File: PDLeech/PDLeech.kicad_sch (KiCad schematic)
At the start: 12 parts

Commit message: schematic finished
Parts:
- removed R?: 270k, -Passive:R_0603, symbol -Passive:R
- removed R?: 51k, -Passive:R_0603, symbol -Passive:R
- added Q1, Q2, Q3, Q4: BSS84, Package_TO_SOT_SMD:SOT-23, symbol Transistor_FET:BSS84
- added R1, R2: 1k, symbol Device:R
- added R3: 270k, symbol Device:R
- added R4: 51k, symbol Device:R
- gave numbers to parts that had none: 10
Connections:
- net +5V: now also R3.1
- net GND: now also R4.2
- net CC2_IN: now reaches JP2.1 (A), P1.B5 (VCONN)
- net CC2_IN: now also Q3.3 (D), R2.1
- net CC2_OUT: now reaches J1.B5 (CC2), JP2.2 (C)
- net CC2_OUT: now also Q4.3 (D)
- net CC2_G: now reaches JP2.3 (B)
- net CC2_G: now also Q3.1 (G), Q4.1 (G), R2.2
- net at U1.5 (FB): now also R3.2, R4.1
- net CC1_OUT: now reaches J1.A5 (CC1), JP1.2 (C)
- net CC1_OUT: now also Q2.3 (D)
- net D+: now reaches J1.A6 (D+), J1.B6 (D+), P1.A6 (D+)
- net D+: now also J2.3 (D+)
- net D-: now reaches J1.A7 (D-), J1.B7 (D-), P1.A7 (D-)
- net D-: now also J2.2 (D-)
- net CC1_IN: now reaches JP1.1 (A), P1.A5 (CC)
- net CC1_IN: now also Q1.3 (D), R1.1
- net CC1_G: now reaches JP1.3 (B)
- net CC1_G: now also Q1.1 (G), Q2.1 (G), R1.2
- new net: Q1.2 (S), Q2.2 (S)
- new net: Q3.2 (S), Q4.2 (S)
- no-connect marks 3 -> 1
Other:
- note removed: "add switching circuit"
- moved on the sheet: C1, C2, C3, J1, J2, JP1, JP2, L1, P1, U1

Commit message: updated schematic
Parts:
- removed R1: 1k, symbol Device:R
- added R?: 4.1k, symbol Device:R
- added R? (x2): 1k, symbol Device:R
- R2: value 1k -> 4.1k
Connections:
- net CC1_G: now also R?.1; no longer Q1.1 (G), Q2.1 (G)
- net CC2_G: now also R2.1; no longer Q3.1 (G), Q4.1 (G), R2.2
- net CC2_IN: no longer R2.1
- net GND: now also R?.2, R?.2
- new net: Q1.1 (G), Q2.1 (G), R?.1, R?.2
- new net: Q3.1 (G), Q4.1 (G), R2.2, R?.1
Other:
- moved on the sheet: Q1, Q2, Q3, Q4, R2

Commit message: added some footprtints
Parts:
- J1: footprint (none) -> Connector_USB:USB_C_Receptacle_Amphenol_12401548E4-2A
- J2: footprint (none) -> USB-A:SAMTEC_USB-A-S-X-X-SM2
- JP1, JP2: footprint (none) -> Jumper:SolderJumper-3_P1.3mm_Bridged12_RoundedPad1.0x1.5mm_NumberLabels
- R1, R2, R4: renamed from R?; footprint (none) -> Resistor_SMD:R_0603_1608Metric_Pad0.98x0.95mm_HandSolder
- R3: renamed from R2; footprint (none) -> Resistor_SMD:R_0603_1608Metric_Pad0.98x0.95mm_HandSolder
- R5: renamed from R3; footprint (none) -> Resistor_SMD:R_0603_1608Metric_Pad0.98x0.95mm_HandSolder
- R6: renamed from R4; footprint (none) -> Resistor_SMD:R_0603_1608Metric_Pad0.98x0.95mm_HandSolder

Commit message: selected all footprints
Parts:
- J1: value USB_C_Receptacle -> TYPEC-324DBW-ACP24A
- P1: value USB_C_Plug -> U261-241N-4BC2LS; footprint (none) -> type-c_plug:USB-C-SMD_XKB_U261-241N-4BC2LS
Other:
- note added: "https://www.lcsc.com/product-detail/USB-Connectors_XKB-Connectivity-U261-241N-4BC2LS_C2880648.html"
- note added: "https://www.lcsc.com/product-detail/USB-Connectors_XUNPU-TYPEC-324DBW-ACP24A_C2840399.html"
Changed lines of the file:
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@@
+    (stroke (width 0) (type default) (color 0 0 0 0))
+  )
+  (wire (pts (xy 22.225 32.385) (xy 23.495 32.385))
     (stroke (width 0) (type default) (color 0 0 0 0))
   )
@@
     (stroke (width 0) (type default) (color 0 0 0 0))
   )
+  (wire (pts (xy 80.645 32.385) (xy 81.915 32.385))
+    (stroke (width 0) (type default) (color 0 0 0 0))
+  )
   (wire (pts (xy 53.34 64.135) (xy 53.34 56.515))
     (stroke (width 0) (type default) (color 0 0 0 0))
@@
   (wire (pts (xy 161.925 72.39) (xy 161.925 74.93))
     (stroke (width 0) (type default) (color 0 0 0 0))
+  )
+  (text "https://www.lcsc.com/product-detail/USB-Connectors_XKB-Connectivity-U261-241N-4BC2LS_C2880648.html"
+    (at 17.78 133.35 0)
+    (effects (font (size 1.27 1.27)) (justify left bottom))
+  )
+  (text "https://www.lcsc.com/product-detail/USB-Connectors_XUNPU-TYPEC-324DBW-ACP24A_C2840399.html"
+    (at 17.78 135.89 0)
+    (effects (font (size 1.27 1.27)) (justify left bottom))
   )
   (text "5V 500mA\n" (at 230.124 48.895 0)
@@
     (effects (font (size 1.27 1.27)) (justify left bottom))
   )
-  (label "CC1_G" (at 23.495 32.385 180)
+  (label "CC1_G" (at 22.225 32.385 180)
     (effects (font (size 1.27 1.27)) (justify right bottom))
   )
-  (label "CC2_G" (at 81.915 32.385 180)
+  (label "CC2_G" (at 80.645 32.385 180)
     (effects (font (size 1.27 1.27)) (justify right bottom))
   )
@@
       (effects (font (size 1.27 1.27)) (justify right))
     )
-    (property "Value" "USB_C_Receptacle" (id 1) (at 104.902 89.5349 0)
+    (property "Value" "TYPEC-324DBW-ACP24A" (id 1) (at 104.902 89.5349 0)
       (effects (font (size 1.27 1.27)) (justify right))
     )
@@
   (symbol (lib_id "-Flag:GND") (at 161.925 76.835 0) (unit 1)
     (in_bom yes) (on_board yes)
-    (property "Reference" "#PWR?" (id 0) (at 161.925 83.185 0)
+    (property "Reference" "#PWR0101" (id 0) (at 161.925 83.185 0)
       (effects (font (size 1.27 1.27)) hide)
     )
@@
     (in_bom yes) (on_board yes) (fields_autoplaced)
     (property "Reference" "P1" (id 0) (at 35.56 51.435 0))
-    (property "Value" "USB_C_Plug" (id 1) (at 35.56 53.975 0))
-    (property "Footprint" "" (id 2) (at 39.37 84.455 0)
+    (property "Value" "U261-241N-4BC2LS" (id 1) (at 35.56 53.975 0))
+    (property "Footprint" "type-c_plug:USB-C-SMD_XKB_U261-241N-4BC2LS" (id 2) (at 39.37 84.455 0)
       (effects (font (size 1.27 1.27)) hide)
     )
@@
     )
     (path "/f0992a04-2738-491f-b5f0-0488ff8c2969"
-      (reference "#PWR?") (unit 1) (value "GND") (footprint "")
+      (reference "#PWR0101") (unit 1) (value "GND") (footprint "")
     )
     (path "/989225e2-7f6b-44a6-8e8d-13851093044b"
@@
     )
     (path "/369f8716-8ba2-4915-a138-c29ccad268b8"
-      (reference "J1") (unit 1) (value "USB_C_Receptacle") (footprint "Connector_USB:USB_C_Receptacle_Amphenol_12401548E4-2A")
+      (reference "J1") (unit 1) (value "TYPEC-324DBW-ACP24A") (footprint "Connector_USB:USB_C_Receptacle_Amphenol_12401548E4-2A")
     )
     (path "/4f67c36c-9553-4237-a40b-64d4286f5052"
@@
     )
     (path "/f8fbfb29-176e-4094-83b6-73d673cd805f"
-      (reference "P1") (unit 1) (value "USB_C_Plug") (footprint "")
+      (reference "P1") (unit 1) (value "U261-241N-4BC2LS") (footprint "type-c_plug:USB-C-SMD_XKB_U261-241N-4BC2LS")
     )
     (path "/f356469c-c44f-4f6c-baed-20c76f284af0"

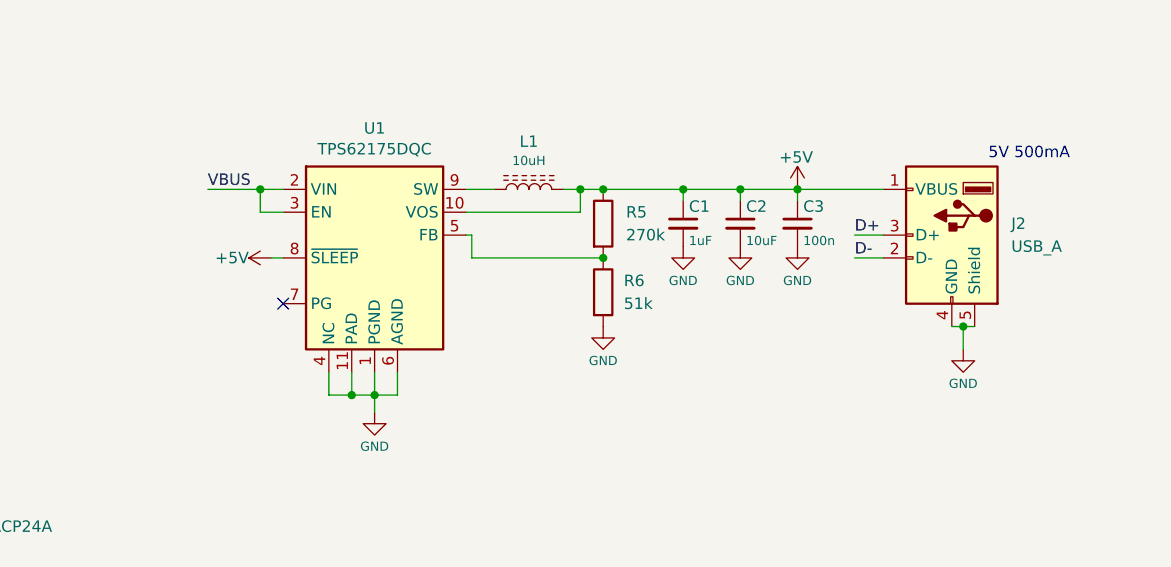
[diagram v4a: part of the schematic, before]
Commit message: schematic complete and footprints selected
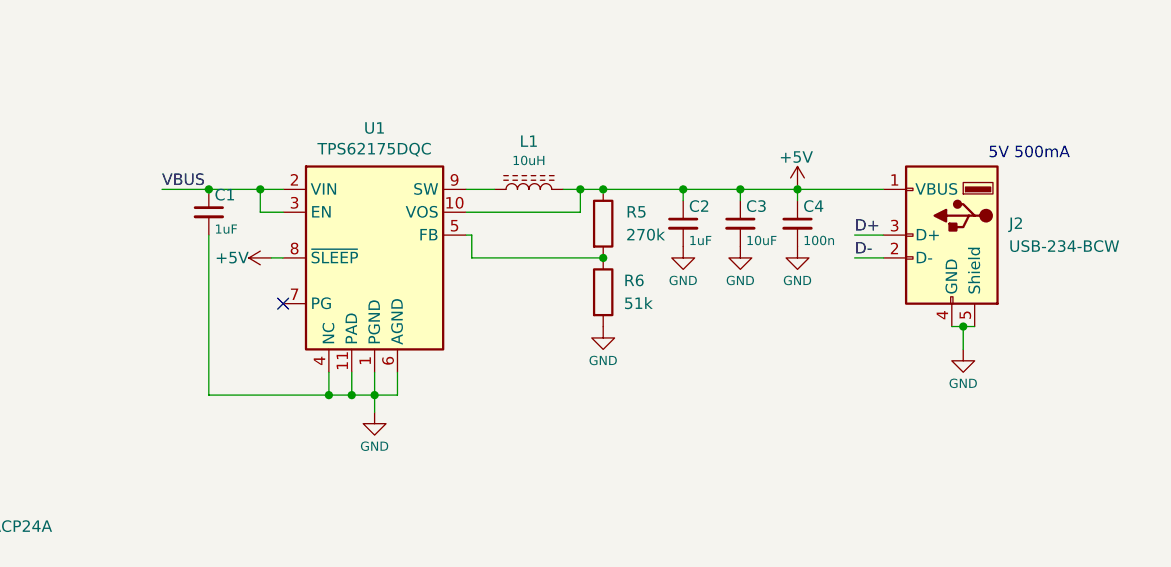
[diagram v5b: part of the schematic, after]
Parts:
- added C1: 1uF, Capacitor_SMD:C_0805_2012Metric_Pad1.18x1.45mm_HandSolder, symbol -Passive:C
- C2: renamed from C1; footprint -Passive:C_0805 -> Capacitor_SMD:C_0805_2012Metric_Pad1.18x1.45mm_HandSolder
- C3: renamed from C2; footprint -Passive:C_0805 -> Capacitor_SMD:C_0805_2012Metric_Pad1.18x1.45mm_HandSolder
- C4: renamed from C3; footprint -Passive:C_0805 -> Capacitor_SMD:C_0805_2012Metric_Pad1.18x1.45mm_HandSolder
- J2: value USB_A -> USB-234-BCW
- L1: footprint -Passive:L_4012 -> Ind-4012:L_4012
- U1: footprint -Chip:WSON-10-1EP_2x3mm_P0.5mm_EP0.84x2.4mm -> TPS62175DQC:WSON-10-1EP_2x3mm_P0.5mm_EP0.84x2.4mm
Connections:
- net GND: now also C1.2
- net VBUS: now also C1.1
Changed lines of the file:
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@@
   (junction (at 196.215 52.07) (diameter 0) (color 0 0 0 0)
   )
+  (junction (at 156.845 74.93) (diameter 0) (color 0 0 0 0)
+  )
   (junction (at 208.915 52.07) (diameter 0) (color 0 0 0 0)
   )
@@
   )
   (junction (at 63.5 125.095) (diameter 0) (color 0 0 0 0)
+  )
+  (junction (at 143.51 52.07) (diameter 0) (color 0 0 0 0)
   )
   (junction (at 95.25 32.385) (diameter 0) (color 0 0 0 0)
@@
     (stroke (width 0) (type default) (color 0 0 0 0))
   )
+  (wire (pts (xy 143.51 74.93) (xy 156.845 74.93))
+    (stroke (width 0) (type default) (color 0 0 0 0))
+  )
   (wire (pts (xy 50.8 64.135) (xy 53.34 64.135))
     (stroke (width 0) (type default) (color 0 0 0 0))
@@
     (stroke (width 0) (type default) (color 0 0 0 0))
   )
-  (wire (pts (xy 143.383 52.07) (xy 149.225 52.07))
+  (wire (pts (xy 138.303 52.07) (xy 143.51 52.07))
     (stroke (width 0) (type default) (color 0 0 0 0))
   )
@@
     (stroke (width 0) (type default) (color 0 0 0 0))
   )
+  (wire (pts (xy 143.51 52.07) (xy 149.225 52.07))
+    (stroke (width 0) (type default) (color 0 0 0 0))
+  )
   (wire (pts (xy 99.695 32.385) (xy 112.395 32.385))
     (stroke (width 0) (type default) (color 0 0 0 0))
@@
   )
   (wire (pts (xy 78.74 71.755) (xy 78.74 74.295))
+    (stroke (width 0) (type default) (color 0 0 0 0))
+  )
+  (wire (pts (xy 143.51 57.15) (xy 143.51 74.93))
     (stroke (width 0) (type default) (color 0 0 0 0))
   )
@@
     (effects (font (size 1.27 1.27)) (justify left bottom))
   )
-  (label "VBUS" (at 143.383 52.07 0)
+  (label "VBUS" (at 138.303 52.07 0)
     (effects (font (size 1.27 1.27)) (justify left bottom))
   )
@@
     (property "Reference" "U1" (id 0) (at 161.925 45.2882 0))
     (property "Value" "TPS62175DQC" (id 1) (at 161.925 47.5996 0))
-    (property "Footprint" "-Chip:WSON-10-1EP_2x3mm_P0.5mm_EP0.84x2.4mm" (id 2) (at 165.735 71.12 0)
+    (property "Footprint" "TPS62175DQC:WSON-10-1EP_2x3mm_P0.5mm_EP0.84x2.4mm" (id 2) (at 165.735 71.12 0)
       (effects (font (size 1.27 1.27)) (justify left) hide)
     )
@@
   (symbol (lib_id "-Passive:C") (at 208.915 55.88 0) (unit 1)
     (in_bom yes) (on_board yes)
-    (property "Reference" "C3" (id 0) (at 209.55 53.975 0)
+    (property "Reference" "C4" (id 0) (at 209.55 53.975 0)
       (effects (font (size 1.27 1.27)) (justify left))
     )
@@
       (effects (font (size 1.016 1.016)) (justify left))
     )
-    (property "Footprint" "-Passive:C_0805" (id 2) (at 209.8802 59.69 0)
+    (property "Footprint" "Capacitor_SMD:C_0805_2012Metric_Pad1.18x1.45mm_HandSolder" (id 2) (at 209.8802 59.69 0)
       (effects (font (size 1.27 1.27)) hide)
     )
     (property "Datasheet" "~" (id 3) (at 208.915 55.88 0)
+      (effects (font (size 1.27 1.27)) hide)
+    )
+    (pin "1")
+    (pin "2")
+  )
+  (symbol (lib_id "-Passive:C") (at 143.51 54.61 0) (unit 1)
+    (in_bom yes) (on_board yes)
+    (property "Reference" "C1" (id 0) (at 144.145 52.705 0)
+      (effects (font (size 1.27 1.27)) (justify left))
+    )
+    (property "Value" "1uF" (id 1) (at 144.145 56.515 0)
+      (effects (font (size 1.016 1.016)) (justify left))
+    )
+    (property "Footprint" "Capacitor_SMD:C_0805_2012Metric_Pad1.18x1.45mm_HandSolder" (id 2) (at 144.4752 58.42 0)
+      (effects (font (size 1.27 1.27)) hide)
+    )
+    (property "Datasheet" "~" (id 3) (at 143.51 54.61 0)
       (effects (font (size 1.27 1.27)) hide)
     )
@@
   (symbol (lib_id "Connector:USB_A") (at 226.06 57.15 0) (mirror y) (unit 1)
     (in_bom yes) (on_board yes) (fields_autoplaced)
-    (property "Reference" "J2" (id 0) (at 232.664 55.8799 0)
+    (property "Reference" "J2" (id 0) (at 232.41 55.8799 0)
       (effects (font (size 1.27 1.27)) (justify right))
     )
-    (property "Value" "USB_A" (id 1) (at 232.664 58.4199 0)
+    (property "Value" "USB-234-BCW" (id 1) (at 232.41 58.4199 0)
       (effects (font (size 1.27 1.27)) (justify right))
     )
@@
   (symbol (lib_id "-Passive:C") (at 196.215 55.88 0) (unit 1)
     (in_bom yes) (on_board yes)
-    (property "Reference" "C1" (id 0) (at 196.85 53.975 0)
+    (property "Reference" "C2" (id 0) (at 196.85 53.975 0)
       (effects (font (size 1.27 1.27)) (justify left))
     )
@@
       (effects (font (size 1.016 1.016)) (justify left))
     )
-    (property "Footprint" "-Passive:C_0805" (id 2) (at 197.1802 59.69 0)
+    (property "Footprint" "Capacitor_SMD:C_0805_2012Metric_Pad1.18x1.45mm_HandSolder" (id 2) (at 197.1802 59.69 0)
       (effects (font (size 1.27 1.27)) hide)
     )
@@
   (symbol (lib_id "-Passive:C") (at 202.565 55.88 0) (unit 1)
     (in_bom yes) (on_board yes)
-    (property "Reference" "C2" (id 0) (at 203.2 53.975 0)
+    (property "Reference" "C3" (id 0) (at 203.2 53.975 0)
       (effects (font (size 1.27 1.27)) (justify left))
     )
@@
       (effects (font (size 1.016 1.016)) (justify left))
     )
-    (property "Footprint" "-Passive:C_0805" (id 2) (at 203.5302 59.69 0)
+    (property "Footprint" "Capacitor_SMD:C_0805_2012Metric_Pad1.18x1.45mm_HandSolder" (id 2) (at 203.5302 59.69 0)
       (effects (font (size 1.27 1.27)) hide)
     )
@@
   (symbol (lib_id "-Flag:GND") (at 161.925 76.835 0) (unit 1)
     (in_bom yes) (on_board yes)
-    (property "Reference" "#PWR0101" (id 0) (at 161.925 83.185 0)
+    (property "Reference" "#PWR05" (id 0) (at 161.925 83.185 0)
       (effects (font (size 1.27 1.27)) hide)
     )
@@
       (effects (font (size 1.016 1.016)))
     )
-    (property "Footprint" "-Passive:L_4012" (id 2) (at 179.07 52.07 90)
+    (property "Footprint" "Ind-4012:L_4012" (id 2) (at 179.07 52.07 90)
       (effects (font (size 1.27 1.27)) hide)
     )
@@
       (reference "#PWR04") (unit 1) (value "+5V") (footprint "")
     )
+    (path "/f0992a04-2738-491f-b5f0-0488ff8c2969"
+      (reference "#PWR05") (unit 1) (value "GND") (footprint "")
+    )
     (path "/b7fa6ec7-c498-419b-95e2-74f90d037e3f"
       (reference "#PWR06") (unit 1) (value "GND") (footprint "")
@@
       (reference "#PWR011") (unit 1) (value "GND") (footprint "")
     )
-    (path "/f0992a04-2738-491f-b5f0-0488ff8c2969"
-      (reference "#PWR0101") (unit 1) (value "GND") (footprint "")
+    (path "/42a94511-b604-4405-86ea-8fb8b1d8d4cd"
+      (reference "C1") (unit 1) (value "1uF") (footprint "Capacitor_SMD:C_0805_2012Metric_Pad1.18x1.45mm_HandSolder")
     )
     (path "/989225e2-7f6b-44a6-8e8d-13851093044b"
-      (reference "C1") (unit 1) (value "1uF") (footprint "-Passive:C_0805")
+      (reference "C2") (unit 1) (value "1uF") (footprint "Capacitor_SMD:C_0805_2012Metric_Pad1.18x1.45mm_HandSolder")
     )
     (path "/cd02239e-c167-47c9-b290-fe5ac68fdfb9"
-      (reference "C2") (unit 1) (value "10uF") (footprint "-Passive:C_0805")
+      (reference "C3") (unit 1) (value "10uF") (footprint "Capacitor_SMD:C_0805_2012Metric_Pad1.18x1.45mm_HandSolder")
     )
     (path "/3fb3938d-ad5f-4a1f-9aeb-7a66c9c14352"
-      (reference "C3") (unit 1) (value "100n") (footprint "-Passive:C_0805")
+      (reference "C4") (unit 1) (value "100n") (footprint "Capacitor_SMD:C_0805_2012Metric_Pad1.18x1.45mm_HandSolder")
     )
     (path "/369f8716-8ba2-4915-a138-c29ccad268b8"
@@
     )
     (path "/4f67c36c-9553-4237-a40b-64d4286f5052"
-      (reference "J2") (unit 1) (value "USB_A") (footprint "USB-A:SAMTEC_USB-A-S-X-X-SM2")
+      (reference "J2") (unit 1) (value "USB-234-BCW") (footprint "USB-A:SAMTEC_USB-A-S-X-X-SM2")
     )
     (path "/e9ff5f11-81d6-44c1-a8fe-360ece4c0b80"
@@
     )
     (path "/fcb783c3-9228-4d47-9296-a4373d1b073a"
-      (reference "L1") (unit 1) (value "10uH") (footprint "-Passive:L_4012")
+      (reference "L1") (unit 1) (value "10uH") (footprint "Ind-4012:L_4012")
     )
     (path "/f8fbfb29-176e-4094-83b6-73d673cd805f"
@@
     )
     (path "/2ffe2d3d-dac7-4da7-a54e-30525b900007"
-      (reference "U1") (unit 1) (value "TPS62175DQC") (footprint "-Chip:WSON-10-1EP_2x3mm_P0.5mm_EP0.84x2.4mm")
-    )
-  )
+      (reference "U1") (unit 1) (value "TPS62175DQC") (footprint "TPS62175DQC:WSON-10-1EP_2x3mm_P0.5mm_EP0.84x2.4mm")
+    )
+  )

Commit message: rough layout complete
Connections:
- net GND: now also J1.S1 (SHIELD), P1.S1 (SHIELD)
- net RX2-: now reaches J1.A10 (RX2-), P1.A10 (RX2-)
- net RX2+: now reaches J1.A11 (RX2+), P1.A11 (RX2+)
- net TX1+: now reaches J1.A2 (TX1+), P1.A2 (TX1+)
- net TX1-: now reaches J1.A3 (TX1-), P1.A3 (TX1-)
- net RX1-: now reaches J1.B10 (RX1-), P1.B10 (RX1-)
- net RX1+: now reaches J1.B11 (RX1+), P1.B11 (RX1+)
- net TX2+: now reaches J1.B2 (TX2+), P1.B2 (TX2+)
- net TX2-: now reaches J1.B3 (TX2-), P1.B3 (TX2-)
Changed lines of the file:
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@@
   (junction (at 227.33 67.31) (diameter 0) (color 0 0 0 0)
+  )
+  (junction (at 63.5 130.81) (diameter 0) (color 0 0 0 0)
   )
   (junction (at 187.325 59.69) (diameter 0) (color 0 0 0 0)
@@
     (stroke (width 0) (type default) (color 0 0 0 0))
   )
-  (wire (pts (xy 27.94 130.81) (xy 101.6 130.81))
+  (wire (pts (xy 27.94 130.81) (xy 63.5 130.81))
     (stroke (width 0) (type default) (color 0 0 0 0))
   )
@@
     (stroke (width 0) (type default) (color 0 0 0 0))
   )
+  (wire (pts (xy 63.5 130.81) (xy 101.6 130.81))
+    (stroke (width 0) (type default) (color 0 0 0 0))
+  )
   (wire (pts (xy 215.265 57.15) (xy 218.44 57.15))
     (stroke (width 0) (type default) (color 0 0 0 0))
@@
     (stroke (width 0) (type default) (color 0 0 0 0))
   )
+  (wire (pts (xy 63.5 130.81) (xy 63.5 132.715))
+    (stroke (width 0) (type default) (color 0 0 0 0))
+  )
   (wire (pts (xy 227.33 67.31) (xy 228.6 67.31))
     (stroke (width 0) (type default) (color 0 0 0 0))
   )
-  (wire (pts (xy 63.5 125.095) (xy 63.5 126.365))
+  (wire (pts (xy 63.5 125.095) (xy 63.5 130.81))
     (stroke (width 0) (type default) (color 0 0 0 0))
   )
@@
   )
   (text "https://www.lcsc.com/product-detail/USB-Connectors_XKB-Connectivity-U261-241N-4BC2LS_C2880648.html"
-    (at 17.78 133.35 0)
+    (at 17.78 139.065 0)
     (effects (font (size 1.27 1.27)) (justify left bottom))
   )
   (text "https://www.lcsc.com/product-detail/USB-Connectors_XUNPU-TYPEC-324DBW-ACP24A_C2840399.html"
-    (at 17.78 135.89 0)
+    (at 17.78 141.605 0)
     (effects (font (size 1.27 1.27)) (justify left bottom))
   )
@@
     (effects (font (size 1.27 1.27)) (justify right bottom))
   )
+  (label "RX1+" (at 52.705 86.995 0)
+    (effects (font (size 1.27 1.27)) (justify left bottom))
+  )
   (label "D-" (at 52.705 71.755 0)
     (effects (font (size 1.27 1.27)) (justify left bottom))
@@
     (effects (font (size 1.27 1.27)) (justify left bottom))
   )
+  (label "TX1+" (at 52.705 94.615 0)
+    (effects (font (size 1.27 1.27)) (justify left bottom))
+  )
   (label "CC1_IN" (at 29.21 24.13 0)
     (effects (font (size 1.27 1.27)) (justify left bottom))
@@
     (effects (font (size 1.27 1.27)) (justify left bottom))
   )
+  (label "RX1-" (at 52.705 84.455 0)
+    (effects (font (size 1.27 1.27)) (justify left bottom))
+  )
+  (label "RX2+" (at 52.705 102.235 0)
+    (effects (font (size 1.27 1.27)) (justify left bottom))
+  )
   (label "D-" (at 215.265 59.69 0)
     (effects (font (size 1.27 1.27)) (justify left bottom))
@@
     (effects (font (size 1.27 1.27)) (justify left bottom))
   )
+  (label "RX2-" (at 52.705 99.695 0)
+    (effects (font (size 1.27 1.27)) (justify left bottom))
+  )
+  (label "TX2-" (at 52.705 107.315 0)
+    (effects (font (size 1.27 1.27)) (justify left bottom))
+  )
+  (label "TX2+" (at 52.705 109.855 0)
+    (effects (font (size 1.27 1.27)) (justify left bottom))
+  )
   (label "CC2_G" (at 71.12 45.085 180)
     (effects (font (size 1.27 1.27)) (justify right bottom))
+  )
+  (label "TX1-" (at 52.705 92.075 0)
+    (effects (font (size 1.27 1.27)) (justify left bottom))
   )
   (label "CC1_OUT" (at 57.15 64.135 0)
@@
     (pin "1")
   )
-  (symbol (lib_id "power:GND") (at 63.5 126.365 0) (unit 1)
+  (symbol (lib_id "power:GND") (at 63.5 132.715 0) (unit 1)
     (in_bom yes) (on_board yes)
-    (property "Reference" "#PWR02" (id 0) (at 63.5 132.715 0)
-      (effects (font (size 1.27 1.27)) hide)
-    )
-    (property "Value" "GND" (id 1) (at 63.5 129.921 0))
-    (property "Footprint" "" (id 2) (at 63.5 126.365 0)
-      (effects (font (size 1.27 1.27)) hide)
-    )
-    (property "Datasheet" "" (id 3) (at 63.5 126.365 0)
-      (effects (font (size 1.27 1.27)) hide)
-    )
+    (property "Reference" "#PWR02" (id 0) (at 63.5 139.065 0)
+      (effects (font (size 1.27 1.27)) hide)
+    )
+    (property "Value" "GND" (id 1) (at 63.5 136.271 0))
+    (property "Footprint" "" (id 2) (at 63.5 132.715 0)
+      (effects (font (size 1.27 1.27)) hide)
+    )
+    (property "Datasheet" "" (id 3) (at 63.5 132.715 0)
+      (effects (font (size 1.27 1.27)) hide)
+    )
